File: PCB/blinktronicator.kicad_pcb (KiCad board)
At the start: 2 copper layers, 23.8 x 23.8 mm, 37 parts, among them P3 RST, P4 SCK, P5 MISO, P6 MOSI, SW2 SW_PUSH, SW3 SW_PUSH, U1 ATTINY85-S, U3 74HC595, U4 74HC595

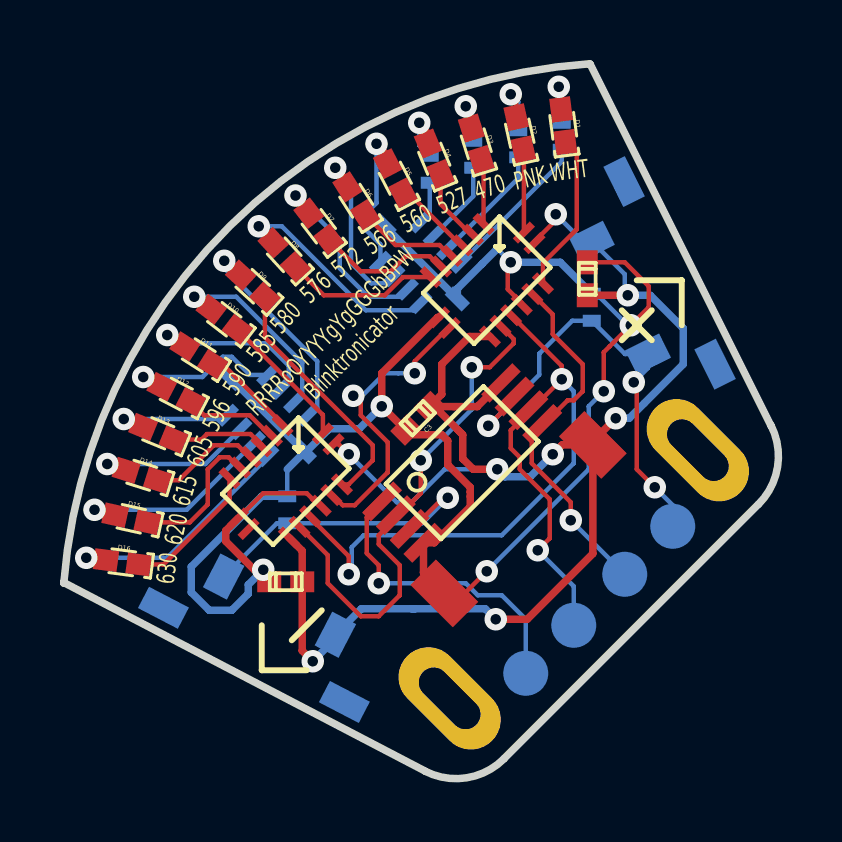
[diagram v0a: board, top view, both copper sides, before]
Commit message: Several minor PCB updates (slots for USB connector, changed silkscreen, etc).
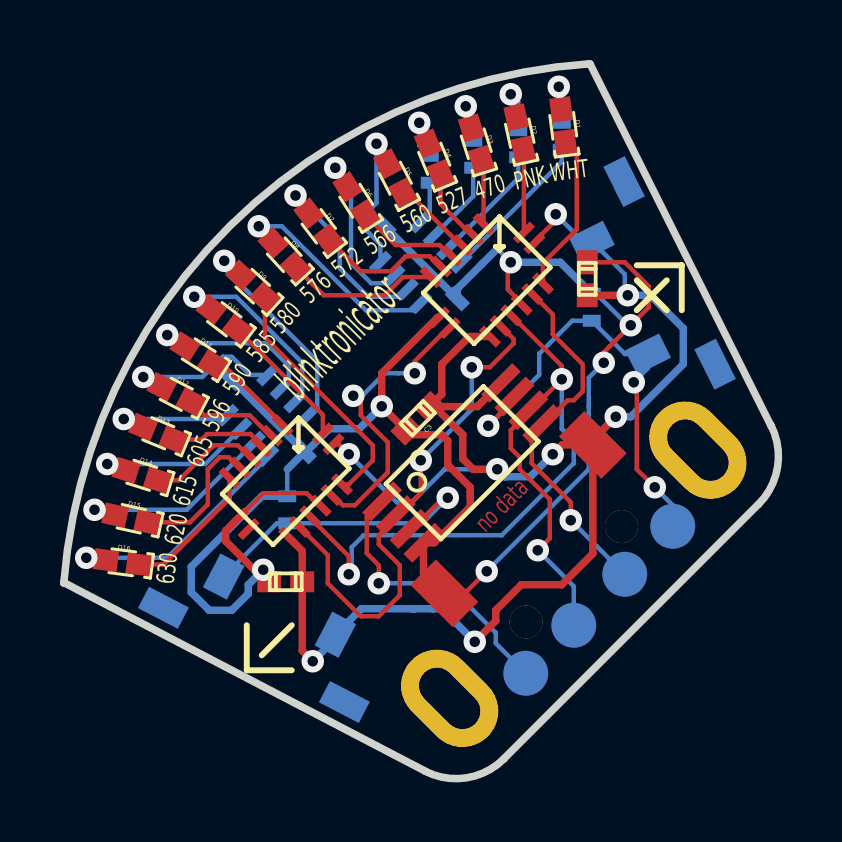
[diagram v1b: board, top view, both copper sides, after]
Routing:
- net N-0000011: track 10.5 -> 9.46 mm
- net VCC: track 54.0 -> 54.9 mm
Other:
- board text added: "blinktronicator"
- board text added: "no data"
- board text removed: "Blinktronicator"
- board text removed: "RRRRoOYYYYgYgGGGbBPW"
